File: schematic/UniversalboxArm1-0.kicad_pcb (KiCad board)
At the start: 2 copper layers, 112 x 57 mm, 201 parts, among them J1 USB_B_Micro, J10 Jack-DC, J100 Conn_02x02_Odd_Even, J110 Conn_01x03_Male, J120 Conn_02x04_Counter_Clockwise, J121 Conn_01x02_Male, J20 AVR-ISP-6, J50 Conn_01x14_Female, J60 Conn_01x06_Female, J61 Conn_02x08_Odd_Even, J90 Conn_02x03_Odd_Even, J91 Conn_02x04_Odd_Even, K90 IM01, K91 IM01, K92 IM01, K93 IM01, Q100 BC817, Q101 BC817, Q102 BC817, Q103 BC817, Q120 IRLML6402, Q20 BCX56-16, Q21 BSS138, Q22 BSS138, Q23 IRLML6402, Q24 IRLML6402, Q25 BSS138, Q50 IRLML6402, Q51 IRLML6402, Q52 BSS138, Q60 BSS138, Q61 BSS138, Q62 BSS138, Q90 BSS138, Q91 BSS138, Q92 BSS138, Q93 BSS138, SW60 SW_SPST, SW61 SW_SPST, SW62 SW_SPST, SW63 SW_SPST, U1 USBLC6-2SC6, U10 MCP16301, U100 BD6221F, U101 BD6221F, U110 MAX3221, U130 TSOP312xx, U2 LP38693MP-3.3, U20 ATtiny861A-SU, U21 REF3020, U22 MCP6542, U50 AT45DB641-S, U60 STM32L452RETx, U61 MCP65R41, Y60 16MHz, Y61 32768Hz

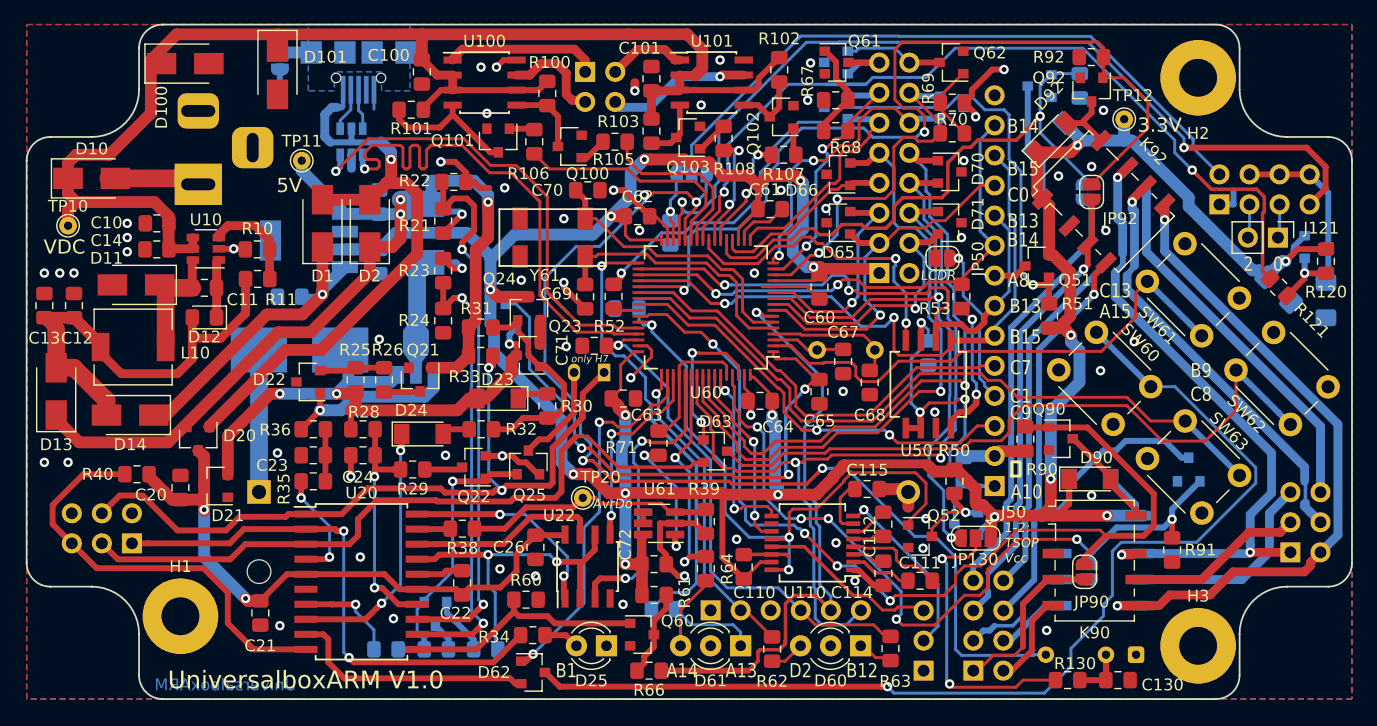
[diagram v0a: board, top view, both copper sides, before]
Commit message: PCB version 0.2 Use 4 layer instead of 2 layer Remove H-bridge drivers Remove step-down converter
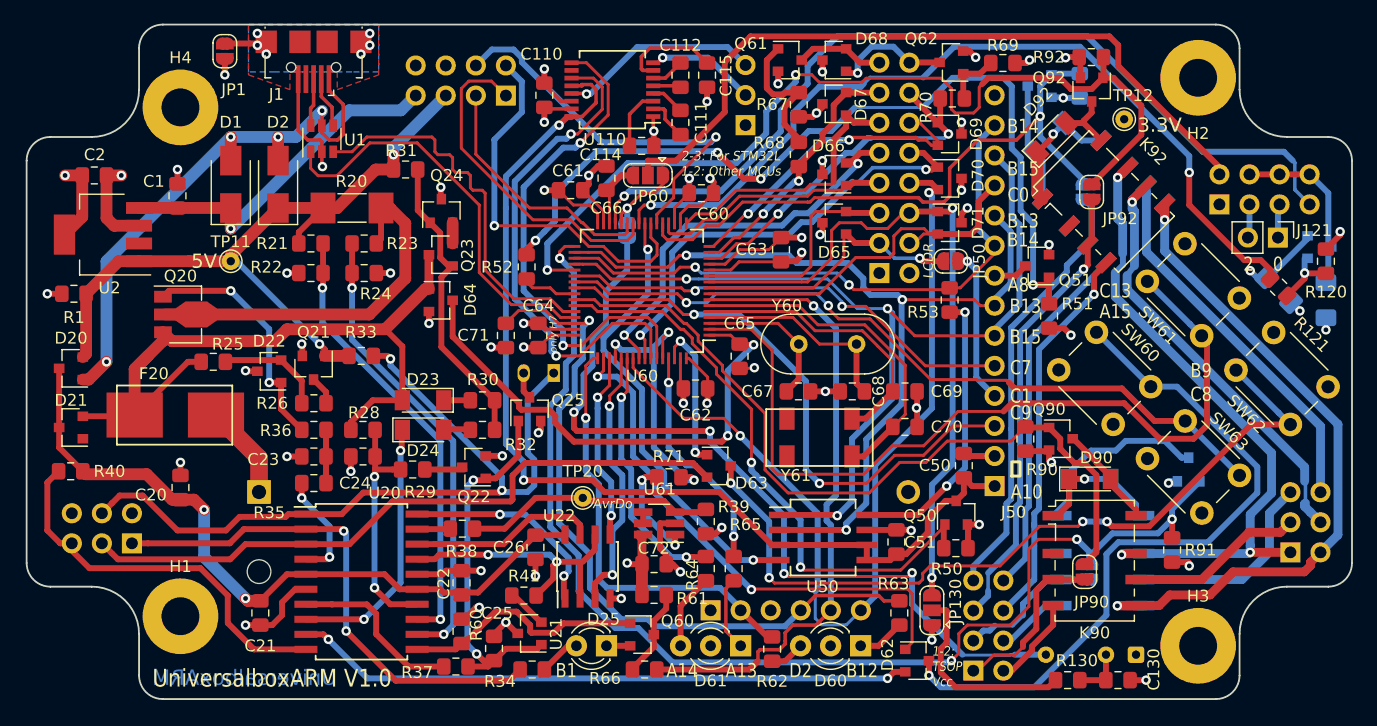
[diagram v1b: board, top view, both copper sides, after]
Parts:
- removed C10, C14: 4.7µF, Capacitor_SMD:C_0805_2012Metric_Pad1.15x1.40mm_HandSolder
- removed C100, C101, C12, C13: 10µF, Capacitor_SMD:C_0805_2012Metric_Pad1.15x1.40mm_HandSolder
- removed C11: 100nF, Capacitor_SMD:C_0805_2012Metric_Pad1.15x1.40mm_HandSolder
- removed D10, D101: MBRA340T3G, Diode_SMD:D_SMA
- removed D100: Z1SMA15, Diode_SMD:D_SMA
- removed D11: B140, Diode_SMD:D_SMA
- removed D12: TS 4148-0805, Diode_SMD:D_0805_2012Metric_Pad1.15x1.40mm_HandSolder
- removed D13, D14: SK14, Diode_SMD:D_SMA
- removed J10: Jack-DC, MalteM:BarrelJack_Horizontal_HEBW21
- removed J100: Conn_02x02_Odd_Even, Connector_PinHeader_2.54mm:PinHeader_2x02_P2.54mm_Vertical
- removed L10: 22µH, Inductor_SMD:L_6.3x6.3_H3
- removed Q100, Q101, Q102, Q103: BC817, Package_TO_SOT_SMD:SOT-23
- removed Q52: BSS138, Package_TO_SOT_SMD:SOT-23
- removed R10: 56kΩ, Resistor_SMD:R_0805_2012Metric_Pad1.15x1.40mm_HandSolder
- removed R100, R101, R102, R103: 1kΩ, Resistor_SMD:R_0805_2012Metric_Pad1.15x1.40mm_HandSolder
- removed R105, R106, R107, R108, R11: 10kΩ, Resistor_SMD:R_0805_2012Metric_Pad1.15x1.40mm_HandSolder
- removed R54: 220kΩ, Resistor_SMD:R_0805_2012Metric_Pad1.15x1.40mm_HandSolder
- removed TP10: TestPoint, TestPoint:TestPoint_THTPad_D1.5mm_Drill0.7mm
- removed U10: MCP16301, Package_TO_SOT_SMD:SOT-23-6
- removed U100, U101: BD6221F, Package_SO:SOIC-8_3.9x4.9mm_P1.27mm
- added H4: MountingHole_Pad, MountingHole:MountingHole_3.2mm_M3_Pad, F.Cu at (117.0, 61.0)
- added J62: Conn_02x04_Odd_Even, Connector_PinHeader_2.54mm:PinHeader_2x04_P2.54mm_Vertical, B.Cu at (144.5, 60.0)
- added JP61: SolderJumper_2_Open, Jumper:SolderJumper-2_P1.3mm_Open_RoundedPad1.0x1.5mm, B.Cu at (154.8, 71.4)
- C1, C2, C25, C50, C51, C66, D64, D67, D68, D69, F20, J1, JP1, JP60, Q20, Q50, R1, R20, R37, R41, R65, U1, U2, U21, Y60: moved to F.Cu
- moved J110 48.5 mm to (164.8, 62.5)
- moved C111 43.7 mm to (159.2, 62.3), turned to 90 degrees
- moved C110 43.3 mm to (147.8, 60.0)
- moved U110 41.9 mm to (153.5, 59.5)
- moved C112 41.6 mm to (159.2, 58.3)
- moved C114 41.5 mm to (156.0, 64.2), turned to 180 degrees
- moved C115 37.5 mm to (161.5, 58.3), turned to 90 degrees
- moved C70 33.4 mm to (178.2, 88.0)
- moved D62 32.5 mm to (179.2, 107.8)
- moved C69 28.2 mm to (178.2, 85.0), turned to 0 degrees
- moved Y61 28.2 mm to (173.8, 90.5)
- moved R1 26.9 mm to (108.0, 76.8), turned to 180 degrees
- moved C2 25.2 mm to (109.7, 66.8), turned to 180 degrees
- moved Q20 20.2 mm to (117.0, 78.5), turned to 0 degrees
- moved C64 19.5 mm to (147.2, 80.3), turned to 90 degrees
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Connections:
- net Net-(C1-Pad1) renamed /VccBase
- C50 pad 1: Net-(C50-Pad1) -> /PerEnablePower
- C51 pad 1: Net-(C50-Pad1) -> /PerEnablePower
- D65 pad 1: /ADC1 -> /ADC2
- D67 pad 1: /Tim2Ch2 -> /UsartExtRx
- D67 pad 2: /UsartExtRx -> /Tim2Ch2
- D69 pad 1: /UsartExtTx -> /Tim2Ch1
- D69 pad 2: /Tim2Ch1 -> /UsartExtTx
- D71 pad 2: /ADC2 -> /ADC1
- J50 pad 1: Net-(C50-Pad1) -> /PerEnablePower
- J61 pad 3: /ADC1 -> /ADC2
- J61 pad 4: /ADC2 -> /ADC1
- Q50 pad 1: Net-(Q50-Pad1) -> /DisablePower
- Q50 pad 3: Net-(C50-Pad1) -> /PerEnablePower
- R50 pad 2: Net-(Q50-Pad1) -> /DisablePower
- U130 pad 3: /Usart3RxOrIr -> /IrRec
- U50 pad 3: Net-(C50-Pad1) -> /PerEnablePower
- U50 pad 5: Net-(C50-Pad1) -> /PerEnablePower
- U50 pad 6: Net-(C50-Pad1) -> /PerEnablePower
- U60 pad 33: Net-(R65-Pad2) -> /Relais2
- U60 pad 43: /PerEnablePower -> /DisablePower
- U60 pad 61: /Relais2 -> Net-(R65-Pad2)
- Y61 pad 1: Net-(C69-Pad1) -> Net-(C70-Pad1)
- Y61 pad 2: Net-(C70-Pad1) -> Net-(C69-Pad1)
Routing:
- net +3V3: track 290.2 -> 87.2 mm, vias 17 -> 18
- net +VDC: track 120.7 -> 0.00 mm
- net /Usart3RxOrIr: track 91.8 -> 8.83 mm, vias 4 -> 1
- net /IrRec: track 0.00 -> 71.0 mm, vias 0 -> 4
- net /DisablePower: track 0.00 -> 50.3 mm, vias 0 -> 2
- net GND: track 90.7 -> 138.5 mm, vias 61 -> 53
- net Net-(C12-Pad1): track 38.5 -> 0.00 mm
- net /Relais2: track 65.2 -> 101.7 mm, vias 6 -> 4
- net /PerEnablePower: track 53.6 -> 88.5 mm, vias 3 -> 2
- net Net-(C50-Pad1): track 33.4 -> 0.00 mm, vias 3 -> 0
- net Net-(D62-Pad3): track 91.3 -> 59.7 mm
- net /AvrInt0: track 21.1 -> 52.4 mm, vias 0 -> 2
- net /Rs232Rx: track 15.6 -> 42.8 mm
- net /Spi2Mosi: track 53.1 -> 80.1 mm, vias 2 -> 3
- net /Rs232Tx: track 15.7 -> 42.7 mm
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- added copper zone on In2.Cu, net +3V3
- added copper zone on F.Cu, net /ShieldGND
- added copper zone on In1.Cu, net GND
- removed copper zone on B.Cu, net GND
- removed copper zone on F.Cu, net GND
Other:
- copper layers 2 -> 4
- board text added: "A1"
- board text added: "The design rule check is expected to find 6 errors"
- board text removed: "Motor1"
- board text removed: "Motor2"
- board text removed: "Only F4, F7, H7"
- board text removed: "The design rule check is expected to find 7 errors"
- board text removed: "VDC"

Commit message: Revision - 0.3. Send to production.
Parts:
- added C4: 100µF, Capacitor_SMD:C_1206_3216Metric_Pad1.33x1.80mm_HandSolder, F.Cu at (116.8, 70.8)
- added D3: SK14, Diode_SMD:D_SMA, F.Cu at (122.2, 73.5)
- added H5: MountingHole_Pad, MountingHole:MountingHole_3.2mm_M3_Pad, F.Cu at (113.7, 95.0)
- C120: footprint Capacitor_SMD:C_1206_3216Metric_Pad1.42x1.75mm_HandSolder -> Capacitor_SMD:C_1206_3216Metric_Pad1.33x1.80mm_HandSolder; moved to F.Cu
- C3: renamed from C121; footprint Capacitor_SMD:C_1206_3216Metric_Pad1.42x1.75mm_HandSolder -> Capacitor_SMD:C_1206_3216Metric_Pad1.33x1.80mm_HandSolder; moved to F.Cu
- Q120: moved to F.Cu
- U110: footprint Package_SO:SSOP-16_5.3x6.2mm_P0.65mm -> MalteM:SSOP-16_5.3x6.2mm_P0.65mm_Handsolder
- U60: footprint Package_QFP:LQFP-64_10x10mm_P0.5mm -> MalteM:LQFP-64_10x10mm_P0.5mm_Handsoldering
- moved C3 102.6 mm to (107.2, 78.1), turned to 90 degrees
- moved R40 15.6 mm to (121.0, 100.0), turned to 270 degrees
- moved R121 13.4 mm to (201.6, 65.6), turned to 90 degrees
- moved J20 6.00 mm to (108.8, 93.5), turned to 180 degrees
- moved JP1 5.09 mm to (123.9, 60.2), turned to 0 degrees
- moved TP11 3.91 mm to (124.2, 76.5)
- moved R120 3.54 mm to (211.6, 76.8)
- moved C20 2.72 mm to (119.0, 95.0)
- moved R1 2.63 mm to (110.6, 76.6), turned to 0 degrees
- moved C1 2.59 mm to (114.8, 66.8), turned to 0 degrees
- moved J91 1.21 mm to (183.5, 107.5)
- moved JP61 1.20 mm to (154.8, 72.6)
- moved J90 0.80 mm to (210.0, 98.6)
- moved C50 0.75 mm to (183.2, 90.5)
- moved C110 0.75 mm to (147.0, 60.0)
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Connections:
- net Net-(D62-Pad1) renamed /KeyLeft
- net Net-(D63-Pad1) renamed /KeyRight
- net Net-(SW61-Pad1) renamed /KeyUp
- net Net-(SW63-Pad1) renamed /KeyDown
- net Net-(U50-Pad4) renamed /FlashCS
- J61 pad 15: Net-(D68-Pad2) -> Net-(D68-Pad1)
- J61 pad 16: Net-(D68-Pad1) -> Net-(D68-Pad2)
- J62 pad 1: /Motor1R -> /Motor1F
- J62 pad 3: /Motor1F -> /Motor1R
- Q61 pad 3: Net-(D68-Pad2) -> Net-(D68-Pad1)
- Q62 pad 3: Net-(D68-Pad1) -> Net-(D68-Pad2)
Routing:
- net Net-(Q120-Pad1): track 5.60 -> 20.7 mm, vias 1 -> 0
- net /EspPowerEnable: track 72.1 -> 57.3 mm
- net /AvrMosi: track 67.4 -> 78.8 mm
- net /AvrMiso: track 43.8 -> 52.8 mm
- net Net-(J20-Pad5): track 33.1 -> 24.3 mm
- net /Motor1R: track 28.5 -> 22.0 mm
- net GND: track 138.5 -> 144.9 mm
- net /VccBase: track 29.8 -> 35.5 mm
- net +3V3: track 87.2 -> 83.1 mm
- net Net-(D62-Pad3): track 59.7 -> 56.7 mm
- net /EspRx: track 75.2 -> 78.1 mm
- net Net-(J90-Pad2): track 58.9 -> 56.1 mm
- net /VccAVR: track 60.8 -> 63.1 mm, vias 2 -> 4
- net /Motor2F: track 33.2 -> 31.0 mm
- net Net-(J90-Pad1): track 56.4 -> 54.5 mm
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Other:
- board text added: "A5"
- board text added: "A6"
- board text added: "A7"
- board text added: "A9"
- board text added: "ADC1"
- board text added: "ADC2"
- board text added: "ADC3"
- board text added: "ADC4"
- board text added: "B0"
- board text added: "B2|11"
- board text added: "B6"
- board text added: "B7"
- board text added: "C6"
- board text added: "DAC1"
- board text added: "For printout: Length is 120mm"
- board text added: "If U130 is used"
- board text added: "MISO1"
- board text added: "MOSI1"
- board text added: "PB10"
- board text added: "RX1"
- board text added: "RX2"
- board text added: "RX3"
- board text added: "SCK1"
- board text added: "T2C1"
- board text added: "T2C2"
- board text added: "TX1"
- board text added: "TX2"
- board text added: "TX3"
- board text added: "The design rule check is expected to find 6 errors The cutouts in layer In1 and In2 are for easier finding solder bridges with a strong light through the PCB, when soldering by hand."
- board text added: "VB"
- board text added: "only non L4"
- board text removed: "RX"
- board text removed: "TX"
- board text removed: "The design rule check is expected to find 6 errors"

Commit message: Update schematic, replace resistor by diode Also make the schematic more easy to read
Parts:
- R62, R64: value 330Ω -> 180Ω
- U61: value MCP65R41 -> MCP65R41T-1202E
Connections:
- net Net-(R64-Pad2) renamed /Led2green
- net Net-(R65-Pad2) renamed /Led2Red

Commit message: Update schematic to version 1 revision 0.5 Reflecting issues found while getting pcb to work
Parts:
- C23: value 1µF -> 10µF
- R30: value 1MΩ -> 220kΩ
- R35: value 150Ω -> 330Ω

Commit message: Schematic: Revision 0.8 Workaround for issues with the crystals Reduce the value of two resistors
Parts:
- C67, C68: value 22pF -> 10pF
- C69, C70: value 4.7pF -> 22pF
- R120, R50: value 220kΩ -> 56kΩ
- Y60: value 16MHz -> 32768Hz
- Y61: value 32768Hz -> 8MHz
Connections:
- net /AvrOutx renamed /AvrOutResetArm
